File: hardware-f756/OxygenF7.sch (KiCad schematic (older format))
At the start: 39 parts, among them J1 Conn_01x04, J2 USB_C_2.0, SW1 SW_Push, SW2 SW_Push, U1 STM32F756VGTx, U2 XC6220B331MR, Y1 8Mhz

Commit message: Add more pull-up/pull-down resistors and 128MB flash memory
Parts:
- added R16: 100k, Resistor_SMD:R_0805_2012Metric, symbol Device:R_US
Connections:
- net GND: now also R16.2
- net LED1: now also U1.2 (PE3); no longer U1.1 (PE2)
- net LED2: now also U1.3 (PE4); no longer U1.2 (PE3)
- net SPI1_MISO: now also R16.1
- net QUADSPI_IO3: now reaches U1.23 (PA1)
- net QUADSPI_SCLK: now reaches U1.36 (PB2)
- net QUADSPI_IO0: now reaches U1.58 (PD11)
- net QUADSPI_IO1: now reaches U1.59 (PD12)
- net UART8_RX: now reaches U1.97 (PE0)
- net UART8_TX: now reaches U1.98 (PE1)
- net USART1_RX: no longer names the net of U1.93 (PB7)
- net USART1_TX renamed QUADSPI_CS
- new net QUADSPI_IO2: U1.1 (PE2)
- no-connect marks 38 -> 33
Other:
- note added: "Ensure that MISO is pulled low\nwhen no chips are selected"
- note added: "SPI1 Pull-Down"
- note removed: "Unused pins must be grounded"
- moved on the sheet: R7, R8
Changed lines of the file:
@@
 Text GLabel 3300 3850 2    50   Output ~ 0
 I2C1_SCL
-Wire Wire Line
-	3300 3650 3200 3650
 Text GLabel 3300 2750 2    50   BiDi ~ 0
 SWCLK
@@
 Text GLabel 1400 6150 0    50   Input ~ 0
 ULTRA_ECHO
-Text Notes 1500 650  0    50   Italic 0
-Unused pins must be grounded
 Text GLabel 1400 5350 0    50   BiDi ~ 0
 GPIO_1
@@
 	1    0    0    -1
 $EndComp
-Text GLabel 1400 3250 0    50   Output ~ 0
+Text GLabel 1350 3350 0    50   Output ~ 0
 LED1
-Text GLabel 1400 3350 0    50   Output ~ 0
+Text GLabel 1350 3450 0    50   Output ~ 0
 LED2
-Text Notes 7150 3350 0    50   ~ 10
+Text Notes 7150 3200 0    50   ~ 10
 I2C Pull-Ups
 Wire Notes Line
-	7150 4150 8350 4150
-Wire Notes Line
-	7150 3400 7150 4150
-Wire Notes Line
-	8350 3400 7150 3400
-Wire Notes Line
-	8350 4150 8350 3400
-Wire Wire Line
-	8050 4050 8050 3950
-Wire Wire Line
-	7600 4050 8050 4050
-Text GLabel 7600 4050 0    50   BiDi ~ 0
+	7150 4000 8350 4000
+Wire Notes Line
+	7150 3250 7150 4000
+Wire Notes Line
+	8350 3250 7150 3250
+Wire Notes Line
+	8350 4000 8350 3250
+Wire Wire Line
+	8050 3900 8050 3800
+Wire Wire Line
+	7600 3900 8050 3900
+Text GLabel 7600 3900 0    50   BiDi ~ 0
 I2C1_SCL
 Wire Wire Line
-	7600 3950 7700 3950
-Text GLabel 7600 3950 0    50   BiDi ~ 0
+	7600 3800 7700 3800
+Text GLabel 7600 3800 0    50   BiDi ~ 0
 I2C1_SDA
 $Comp
 L power:+3.3V #PWR060
 U 1 1 6077C5A7
-P 8050 3650
-F 0 "#PWR060" H 8050 3500 50  0001 C CNN
-F 1 "+3.3V" H 8065 3823 50  0000 C CNN
-F 2 "" H 8050 3650 50  0001 C CNN
-F 3 "" H 8050 3650 50  0001 C CNN
-	1    8050 3650
+P 8050 3500
+F 0 "#PWR060" H 8050 3350 50  0001 C CNN
+F 1 "+3.3V" H 8065 3673 50  0000 C CNN
+F 2 "" H 8050 3500 50  0001 C CNN
+F 3 "" H 8050 3500 50  0001 C CNN
+	1    8050 3500
 	1    0    0    -1
 $EndComp
@@
 L power:+3.3V #PWR059
 U 1 1 6077BF4A
-P 7700 3650
-F 0 "#PWR059" H 7700 3500 50  0001 C CNN
-F 1 "+3.3V" H 7715 3823 50  0000 C CNN
-F 2 "" H 7700 3650 50  0001 C CNN
-F 3 "" H 7700 3650 50  0001 C CNN
-	1    7700 3650
+P 7700 3500
+F 0 "#PWR059" H 7700 3350 50  0001 C CNN
+F 1 "+3.3V" H 7715 3673 50  0000 C CNN
+F 2 "" H 7700 3500 50  0001 C CNN
+F 3 "" H 7700 3500 50  0001 C CNN
+	1    7700 3500
 	1    0    0    -1
 $EndComp
@@
 L Device:R_US R8
 U 1 1 6077BC5D
-P 8050 3800
-F 0 "R8" H 8118 3846 50  0000 L CNN
-F 1 "4.7k" H 8118 3755 50  0000 L CNN
-F 2 "Resistor_SMD:R_0805_2012Metric" V 8090 3790 50  0001 C CNN
-F 3 "~" H 8050 3800 50  0001 C CNN
-F 4 "RMCF0805FT4K70" H 8050 3800 50  0001 C CNN "Part#"
-	1    8050 3800
+P 8050 3650
+F 0 "R8" H 8118 3696 50  0000 L CNN
+F 1 "4.7k" H 8118 3605 50  0000 L CNN
+F 2 "Resistor_SMD:R_0805_2012Metric" V 8090 3640 50  0001 C CNN
+F 3 "~" H 8050 3650 50  0001 C CNN
+F 4 "RMCF0805FT4K70" H 8050 3650 50  0001 C CNN "Part#"
+	1    8050 3650
 	1    0    0    -1
 $EndComp
@@
 L Device:R_US R7
 U 1 1 6077B843
-P 7700 3800
-F 0 "R7" H 7768 3846 50  0000 L CNN
-F 1 "4.7k" H 7768 3755 50  0000 L CNN
-F 2 "Resistor_SMD:R_0805_2012Metric" V 7740 3790 50  0001 C CNN
-F 3 "~" H 7700 3800 50  0001 C CNN
-F 4 "RMCF0805FT4K70" H 7700 3800 50  0001 C CNN "Part#"
-	1    7700 3800
+P 7700 3650
+F 0 "R7" H 7768 3696 50  0000 L CNN
+F 1 "4.7k" H 7768 3605 50  0000 L CNN
+F 2 "Resistor_SMD:R_0805_2012Metric" V 7740 3640 50  0001 C CNN
+F 3 "~" H 7700 3650 50  0001 C CNN
+F 4 "RMCF0805FT4K70" H 7700 3650 50  0001 C CNN "Part#"
+	1    7700 3650
 	1    0    0    -1
 $EndComp
@@
 Wire Wire Line
 	3200 3950 3300 3950
-Text GLabel 3300 3650 2    50   Output ~ 0
-USART1_TX
 Text GLabel 3300 2250 2    50   Input ~ 0
 VBUS
@@
 Wire Wire Line
 	3200 2550 3300 2550
-Text GLabel 3300 3750 2    50   Input ~ 0
-USART1_RX
-Wire Wire Line
-	3300 3750 3200 3750
 Text GLabel 3300 1550 2    50   BiDi ~ 0
 USART2_TX
@@
 Wire Notes Line
 	9150 2900 9150 2000
-Wire Wire Line
-	1400 3250 1500 3250
-Wire Wire Line
-	1400 3350 1500 3350
 $Comp
 L MCU_ST_STM32F7:STM32F756VGTx U1
@@
 	7000 3400 7000 4550
 NoConn ~ 3200 1350
-NoConn ~ 3200 1450
 NoConn ~ 3200 1650
 NoConn ~ 3200 1750
@@
 NoConn ~ 3200 4750
 NoConn ~ 1500 6050
-NoConn ~ 1500 5950
-NoConn ~ 1500 5850
 NoConn ~ 1500 5750
 NoConn ~ 1500 5450
@@
 NoConn ~ 1500 3650
 NoConn ~ 1500 3550
-NoConn ~ 1500 3450
-NoConn ~ 1500 3150
-NoConn ~ 1500 3050
 NoConn ~ 3200 2150
 NoConn ~ 3200 2350
 NoConn ~ 3200 2850
-NoConn ~ 3200 3250
 NoConn ~ 3200 3350
 NoConn ~ 3200 3450
 NoConn ~ 3200 3550
+Text GLabel 1400 5850 0    50   BiDi ~ 0
+QUADSPI_IO0
+Wire Wire Line
+	1400 5850 1500 5850
+Wire Wire Line
+	1400 5950 1500 5950
+Text GLabel 1400 5950 0    50   BiDi ~ 0
+QUADSPI_IO1
+Text GLabel 1350 3250 0    50   BiDi ~ 0
+QUADSPI_IO2
+Wire Wire Line
+	1350 3250 1500 3250
+Text GLabel 3300 1450 2    50   BiDi ~ 0
+QUADSPI_IO3
+Wire Wire Line
+	3300 1450 3200 1450
+Text GLabel 3300 3250 2    50   Output ~ 0
+QUADSPI_SCLK
+Wire Wire Line
+	3300 3250 3200 3250
+Text GLabel 3300 3650 2    50   BiDi ~ 0
+QUADSPI_CS
+Wire Wire Line
+	3300 3650 3200 3650
+$Comp
+L Device:R_US R16
+U 1 1 60FE8DF0
+P 9100 3550
+F 0 "R16" H 9168 3596 50  0000 L CNN
+F 1 "100k" H 9168 3505 50  0000 L CNN
+F 2 "Resistor_SMD:R_0805_2012Metric" V 9140 3540 50  0001 C CNN
+F 3 "~" H 9100 3550 50  0001 C CNN
+F 4 "RMCF0805FT4K70" H 9100 3550 50  0001 C CNN "Part#"
+	1    9100 3550
+	1    0    0    -1
+$EndComp
+Text GLabel 9000 3400 0    50   Output ~ 0
+SPI1_MISO
+Wire Wire Line
+	9000 3400 9100 3400
+$Comp
+L power:GND #PWR042
+U 1 1 60FF50BF
+P 9100 3700
+F 0 "#PWR042" H 9100 3450 50  0001 C CNN
+F 1 "GND" H 9105 3527 50  0000 C CNN
+F 2 "" H 9100 3700 50  0001 C CNN
+F 3 "" H 9100 3700 50  0001 C CNN
+	1    9100 3700
+	1    0    0    -1
+$EndComp
+Wire Notes Line
+	8500 3250 9400 3250
+Wire Notes Line
+	9400 3250 9400 4000
+Wire Notes Line
+	9400 4000 8500 4000
+Wire Notes Line
+	8500 4000 8500 3250
+Text Notes 8500 3200 0    50   ~ 10
+SPI1 Pull-Down
+Text Notes 8500 4200 0    50   Italic 0
+Ensure that MISO is pulled low\nwhen no chips are selected
+Wire Wire Line
+	1350 3450 1500 3450
+Wire Wire Line
+	1350 3350 1500 3350
+Text GLabel 1350 3050 0    50   Input ~ 0
+UART8_RX
+Text GLabel 1350 3150 0    50   Output ~ 0
+UART8_TX
+Wire Wire Line
+	1350 3150 1500 3150
+Wire Wire Line
+	1350 3050 1500 3050
+NoConn ~ 3200 3750
+NoConn ~ 1500 4050
 $EndSCHEMATC

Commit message: New board layout
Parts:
- D3: Part# 150080BS75000 -> 150080RS75000
- D4: Part# 150080RS75000 -> 150080BS75000
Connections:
- net +5V_BEC: now also D1.2; no longer D1.1
- net GPIO_1: now also U1.89 (PB3); no longer U1.87 (PD6)
- net GPIO_2: now also U1.88 (PD7); no longer U1.86 (PD5)
- net GPIO_3: now also U1.87 (PD6); no longer U1.85 (PD4)
- net GPIO_4: now also U1.86 (PD5); no longer U1.84 (PD3)
- net QUADSPI_IO3: now also U1.60 (PD13); no longer U1.23 (PA1)
- net ULTRA_ECHO: now also U1.67 (PA8); no longer U1.61 (PD14)
- net ULTRA_TRIG: now also U1.69 (PA10); no longer U1.62 (PD15)
- net VBUS: now also D1.1; no longer D1.2
- no-connect marks 33 -> 29
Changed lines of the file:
@@
 Text GLabel 3300 4250 2    50   Input ~ 0
 MPU_INT
-Text GLabel 1400 6250 0    50   Output ~ 0
+Text GLabel 3300 2350 2    50   Output ~ 0
 ULTRA_TRIG
-Text GLabel 1400 6150 0    50   Input ~ 0
+Text GLabel 3300 2150 2    50   Input ~ 0
 ULTRA_ECHO
+Text GLabel 3300 3350 2    50   BiDi ~ 0
+GPIO_1
+Text GLabel 1400 5450 0    50   BiDi ~ 0
+GPIO_2
+Text GLabel 1400 5250 0    50   BiDi ~ 0
+GPIO_4
 Text GLabel 1400 5350 0    50   BiDi ~ 0
-GPIO_1
-Text GLabel 1400 5250 0    50   BiDi ~ 0
-GPIO_2
-Text GLabel 1400 5150 0    50   BiDi ~ 0
 GPIO_3
-Text GLabel 1400 5050 0    50   BiDi ~ 0
-GPIO_4
 Text GLabel 3300 5450 2    50   Input ~ 0
 SDMMC1_DETECT
@@
 F 2 "LED_SMD:LED_0805_2012Metric" H 5400 5250 50  0001 C CNN
 F 3 "~" H 5400 5250 50  0001 C CNN
-F 4 "150080RS75000" H 5400 5250 50  0001 C CNN "Part#"
+F 4 "150080BS75000" H 5400 5250 50  0001 C CNN "Part#"
 	1    5400 5250
 	0    -1   -1   0
@@
 F 2 "LED_SMD:LED_0805_2012Metric" H 4950 5250 50  0001 C CNN
 F 3 "~" H 4950 5250 50  0001 C CNN
-F 4 "150080BS75000" H 4950 5250 50  0001 C CNN "Part#"
+F 4 "150080RS75000" H 4950 5250 50  0001 C CNN "Part#"
 	1    4950 5250
 	0    -1   -1   0
@@
 Wire Wire Line
 	4850 4100 4700 4100
-Text GLabel 4700 4100 0    50   Input ~ 0
+Text GLabel 4700 3500 0    50   Input ~ 0
 +5V_BEC
 $Comp
@@
 Wire Wire Line
 	3300 1550 3200 1550
-Text GLabel 4700 3500 0    50   Input ~ 0
+Text GLabel 4700 4100 0    50   Input ~ 0
 VBUS
 Wire Notes Line
@@
 $EndComp
 Wire Wire Line
-	1500 5050 1400 5050
-Wire Wire Line
-	1400 5150 1500 5150
-Wire Wire Line
-	1500 5250 1400 5250
-Wire Wire Line
-	1400 5350 1500 5350
+	1500 5350 1400 5350
+Wire Wire Line
+	3300 3350 3200 3350
+Wire Wire Line
+	1500 5450 1400 5450
+Wire Wire Line
+	1400 5250 1500 5250
 Wire Wire Line
 	3300 5450 3200 5450
 Wire Wire Line
-	1400 6150 1500 6150
-Wire Wire Line
-	1400 6250 1500 6250
+	3300 2150 3200 2150
+Wire Wire Line
+	3300 2350 3200 2350
 Wire Wire Line
 	3300 4250 3200 4250
@@
 NoConn ~ 3200 4850
 NoConn ~ 3200 4750
-NoConn ~ 1500 6050
 NoConn ~ 1500 5750
-NoConn ~ 1500 5450
 NoConn ~ 1500 4550
 NoConn ~ 1500 4250
@@
 NoConn ~ 1500 3650
 NoConn ~ 1500 3550
-NoConn ~ 3200 2150
-NoConn ~ 3200 2350
 NoConn ~ 3200 2850
-NoConn ~ 3200 3350
-NoConn ~ 3200 3450
-NoConn ~ 3200 3550
 Text GLabel 1400 5850 0    50   BiDi ~ 0
 QUADSPI_IO0
@@
 Wire Wire Line
 	1350 3250 1500 3250
-Text GLabel 3300 1450 2    50   BiDi ~ 0
+Text GLabel 1400 6050 0    50   BiDi ~ 0
 QUADSPI_IO3
 Wire Wire Line
-	3300 1450 3200 1450
+	1400 6050 1500 6050
 Text GLabel 3300 3250 2    50   Output ~ 0
 QUADSPI_SCLK
@@
 NoConn ~ 3200 3750
 NoConn ~ 1500 4050
+NoConn ~ 1500 6150
+NoConn ~ 1500 6250
+NoConn ~ 3200 1450
 $EndSCHEMATC

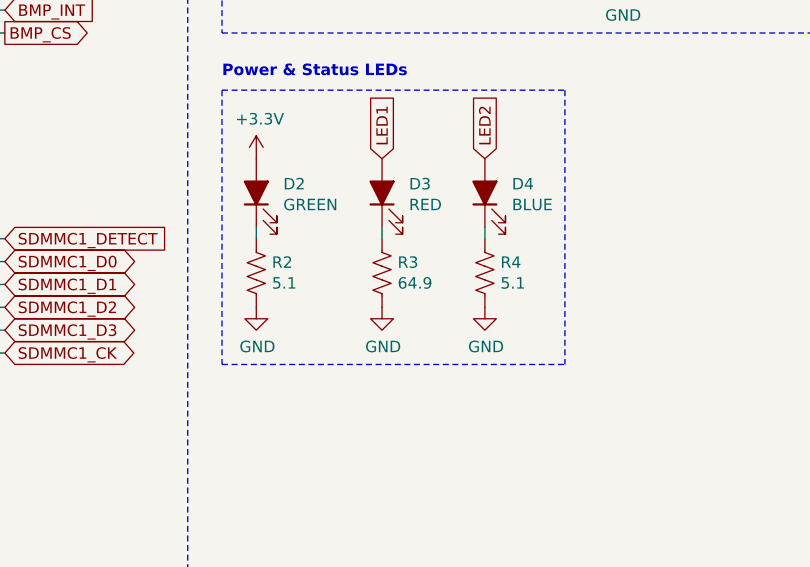
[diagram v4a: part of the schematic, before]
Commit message: Update resistor values for status LED to use only 5mA
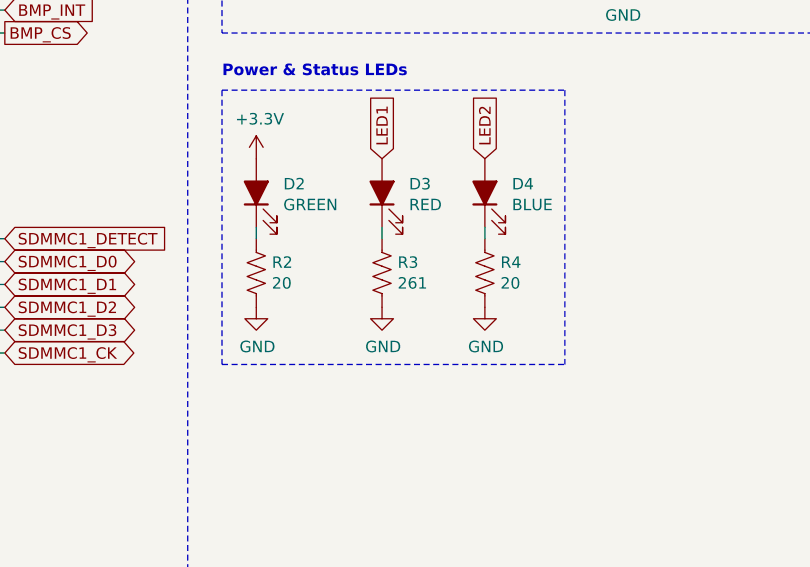
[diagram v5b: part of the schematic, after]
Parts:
- R2, R4: value 5.1 -> 20; Part# RMCF0805FT5R10 -> RMCF0805FT20R0
- R3: value 64.9 -> 261; Part# RMCF0805FT64R9 -> RMCF0805FT261R
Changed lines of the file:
@@
 P 5400 5600
 F 0 "R4" H 5468 5646 50  0000 L CNN
-F 1 "5.1" H 5468 5555 50  0000 L CNN
+F 1 "20" H 5468 5555 50  0000 L CNN
 F 2 "Resistor_SMD:R_0805_2012Metric" V 5440 5590 50  0001 C CNN
 F 3 "~" H 5400 5600 50  0001 C CNN
-F 4 "RMCF0805FT5R10" H 5400 5600 50  0001 C CNN "Part#"
+F 4 "RMCF0805FT20R0" H 5400 5600 50  0001 C CNN "Part#"
 	1    5400 5600
 	1    0    0    -1
@@
 P 4950 5600
 F 0 "R3" H 5018 5646 50  0000 L CNN
-F 1 "64.9" H 5018 5555 50  0000 L CNN
+F 1 "261" H 5018 5555 50  0000 L CNN
 F 2 "Resistor_SMD:R_0805_2012Metric" V 4990 5590 50  0001 C CNN
 F 3 "~" H 4950 5600 50  0001 C CNN
-F 4 "RMCF0805FT64R9" H 4950 5600 50  0001 C CNN "Part#"
+F 4 "RMCF0805FT261R" H 4950 5600 50  0001 C CNN "Part#"
 	1    4950 5600
 	1    0    0    -1
@@
 P 4400 5600
 F 0 "R2" H 4468 5646 50  0000 L CNN
-F 1 "5.1" H 4468 5555 50  0000 L CNN
+F 1 "20" H 4468 5555 50  0000 L CNN
 F 2 "Resistor_SMD:R_0805_2012Metric" V 4440 5590 50  0001 C CNN
 F 3 "~" H 4400 5600 50  0001 C CNN
-F 4 "RMCF0805FT5R10" H 4400 5600 50  0001 C CNN "Part#"
+F 4 "RMCF0805FT20R0" H 4400 5600 50  0001 C CNN "Part#"
 	1    4400 5600
 	1    0    0    -1

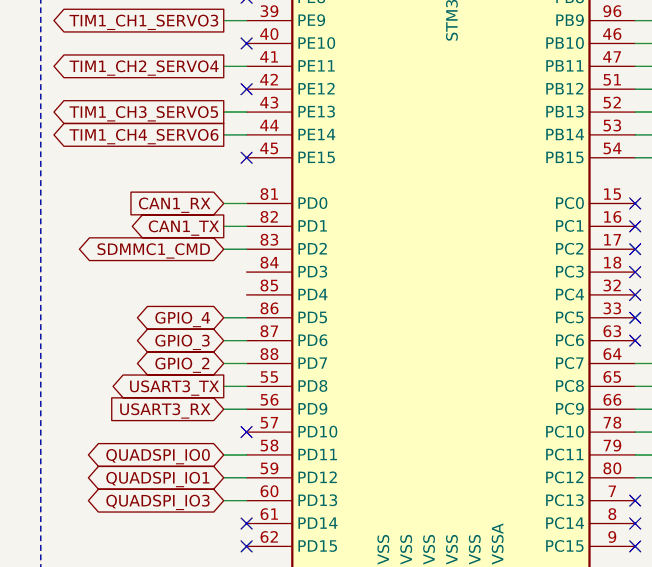
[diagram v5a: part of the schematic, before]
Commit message: Small layout tweaks
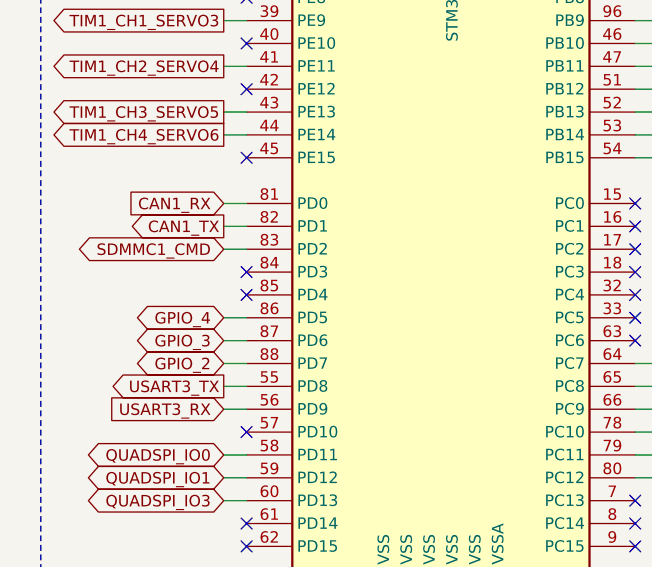
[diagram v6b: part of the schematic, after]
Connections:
- no-connect marks 29 -> 31
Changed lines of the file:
@@
 NoConn ~ 1500 6250
 NoConn ~ 3200 1450
+NoConn ~ 1500 5050
+NoConn ~ 1500 5150
 $EndSCHEMATC

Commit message: Small tweaks
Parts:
- R1: Part# RNCP0805FTD10K0 -> RMCF0805FT10K0
- R16: Part# RMCF0805FT4K70 -> RMCF0805FT100K
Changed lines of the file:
@@
 F 2 "Resistor_SMD:R_0805_2012Metric" V 8190 2640 50  0001 C CNN
 F 3 "~" H 8150 2650 50  0001 C CNN
-F 4 "RNCP0805FTD10K0" H 8150 2650 50  0001 C CNN "Part#"
+F 4 "RMCF0805FT10K0" H 8150 2650 50  0001 C CNN "Part#"
 	1    8150 2650
 	0    -1   -1   0
@@
 F 2 "Resistor_SMD:R_0805_2012Metric" V 9140 3540 50  0001 C CNN
 F 3 "~" H 9100 3550 50  0001 C CNN
-F 4 "RMCF0805FT4K70" H 9100 3550 50  0001 C CNN "Part#"
+F 4 "RMCF0805FT100K" H 9100 3550 50  0001 C CNN "Part#"
 	1    9100 3550
 	1    0    0    -1
